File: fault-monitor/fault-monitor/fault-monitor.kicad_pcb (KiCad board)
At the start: 2 copper layers, 72 x 73.5 mm, 25 parts, among them J1 Conn_01x03, J2 Conn_01x06, J3 Conn_01x02, J4 Conn_01x02, J5 Conn_01x02, J6 Conn_01x02, J7 Conn_01x06, U1 ESP32-DevKitC

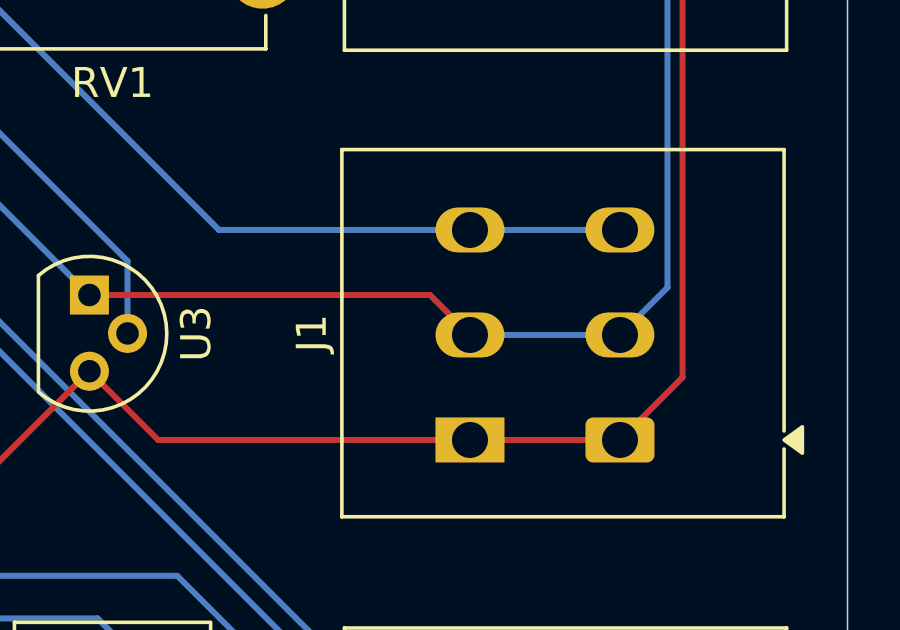
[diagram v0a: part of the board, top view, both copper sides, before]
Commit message: update to use real parts we will order
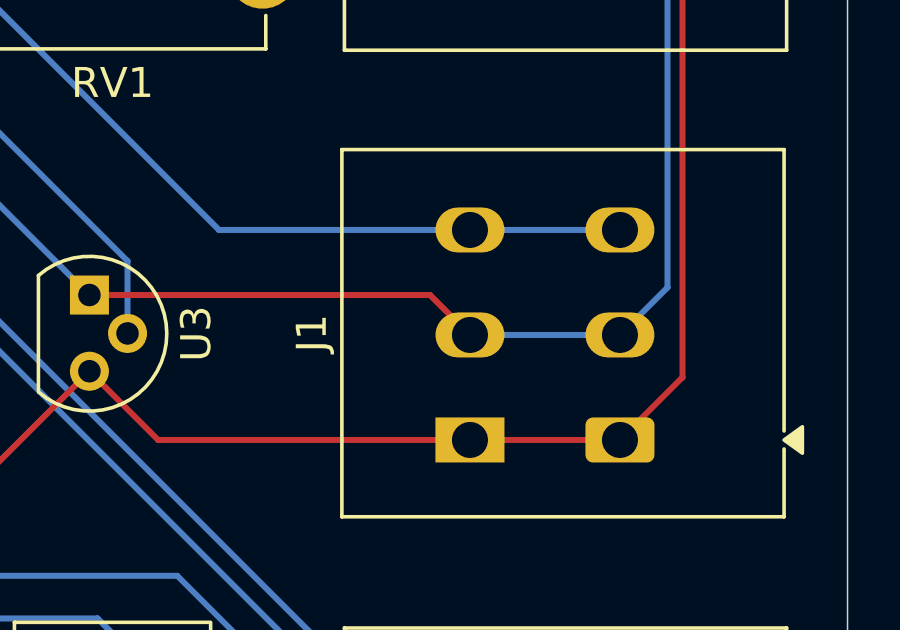
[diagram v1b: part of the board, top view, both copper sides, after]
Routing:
- net GND: track 160.8 -> 158.9 mm
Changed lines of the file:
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@@
-	)
-	(segment
-		(start 110.415 76.05156)
-		(end 109.08344 74.72)
-		(width 0.2)
-		(layer "B.Cu")
-		(net 1)
 	)
 	(segment

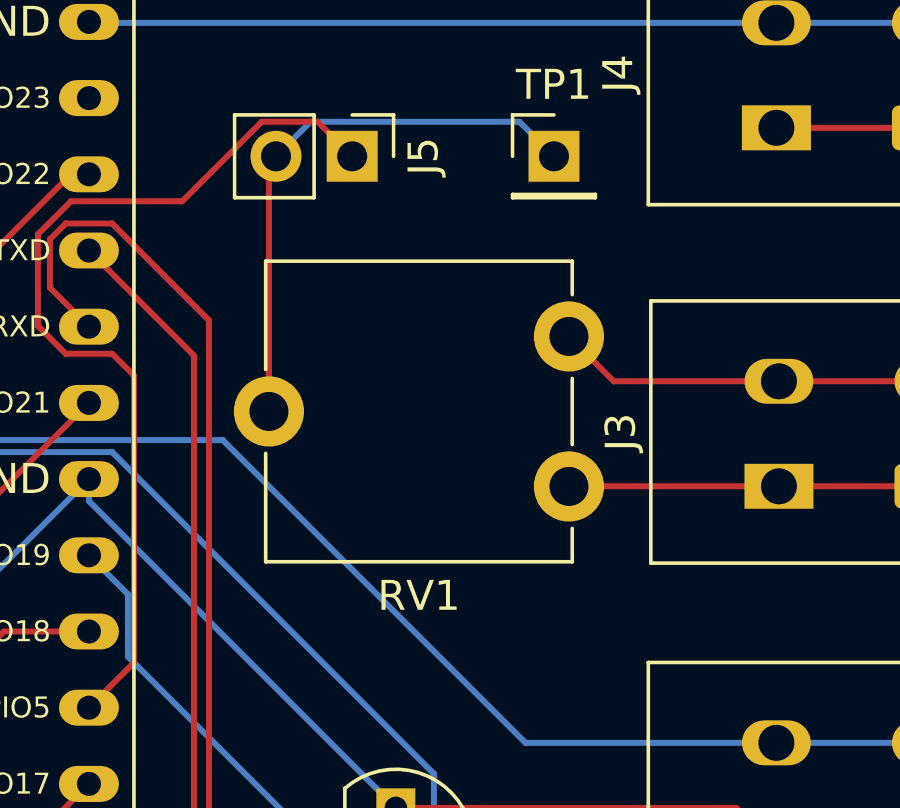
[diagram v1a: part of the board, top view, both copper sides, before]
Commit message: swap pot foot
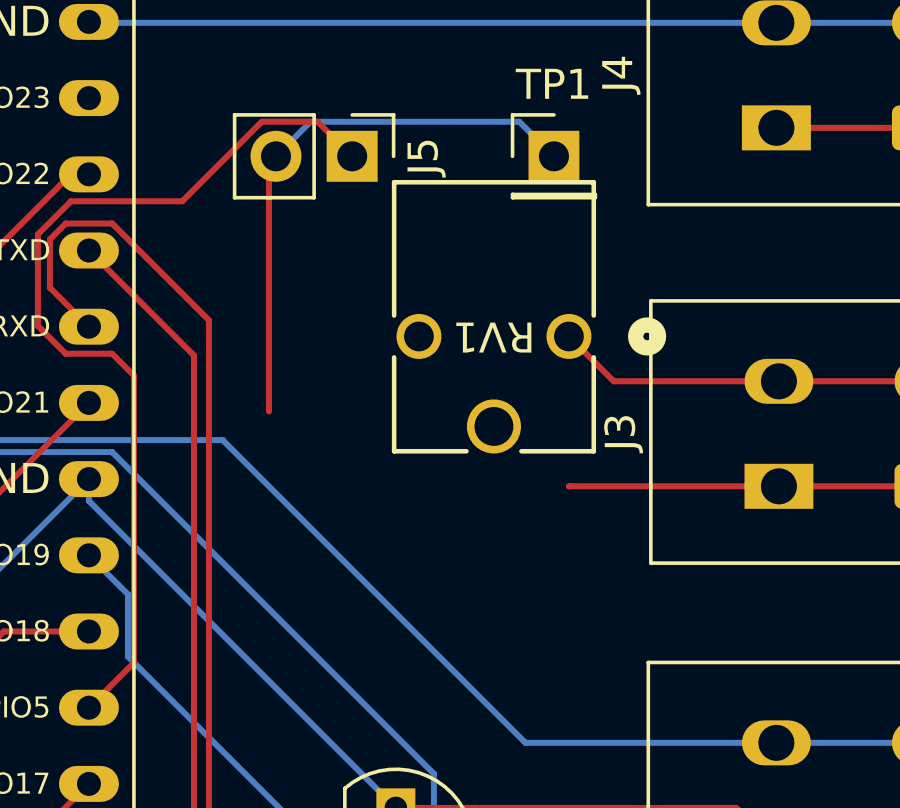
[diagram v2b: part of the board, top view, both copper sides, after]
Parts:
- RV1: footprint Potentiometer_THT:Potentiometer_ACP_CA9-V10_Vertical -> DigiKey:POT_N6L30T0N_AMP
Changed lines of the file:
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@@
 		(embedded_fonts no)
 	)
-	(footprint "Potentiometer_THT:Potentiometer_ACP_CA9-V10_Vertical"
+	(footprint "DigiKey:POT_N6L30T0N_AMP"
 		(layer "F.Cu")
 		(at 103.5 59.005 180)
-		(descr "Potentiometer, vertical, ACP CA9-V10, http://www.acptechnologies.com/wp-content/uploads/2017/05/02-ACP-CA9-CE9.pdf")
-		(tags "Potentiometer vertical ACP CA9-V10")
+		(tags "N6L30T0N-103-3030 ")
 		(property "Reference" "RV1"
-			(at 5 -8.65 0)
+			(at 2.5 0 180)
+			(unlocked yes)
 			(layer "F.SilkS")
 			(effects
@@
 		)
 		(property "Value" "10K"
-			(at 5 3.65 0)
+			(at 2.5 0 180)
+			(unlocked yes)
 			(layer "F.Fab")
 			(effects
@@
 		)
 		(property "Datasheet" "~"
-			(at 0 0 0)
+			(at 0 0 180)
 			(layer "F.Fab")
 			(hide yes)
@@
 		)
 		(property "Description" "Potentiometer"
-			(at 0 0 0)
+			(at 0 0 180)
 			(layer "F.Fab")
 			(hide yes)
@@
 		(attr through_hole)
 		(fp_line
-			(start 10.11 2.51)
-			(end -0.11 2.51)
-			(stroke
-				(width 0.12)
-				(type solid)
-			)
-			(layer "F.SilkS")
-		)
-		(fp_line
-			(start 10.11 -1.104)
-			(end 10.11 2.51)
-			(stroke
-				(width 0.12)
-				(type solid)
-			)
-			(layer "F.SilkS")
-		)
-		(fp_line
-			(start 10.11 -7.51)
-			(end 10.11 -3.896)
-			(stroke
-				(width 0.12)
-				(type solid)
-			)
-			(layer "F.SilkS")
-		)
-		(fp_line
-			(start -0.11 2.51)
-			(end -0.11 1.396)
-			(stroke
-				(width 0.12)
-				(type solid)
-			)
-			(layer "F.SilkS")
-		)
-		(fp_line
-			(start -0.11 -1.396)
-			(end -0.11 -3.604)
-			(stroke
-				(width 0.12)
-				(type solid)
-			)
-			(layer "F.SilkS")
-		)
-		(fp_line
-			(start -0.11 -6.396)
-			(end -0.11 -7.51)
-			(stroke
-				(width 0.12)
-				(type solid)
-			)
-			(layer "F.SilkS")
-		)
-		(fp_line
-			(start -0.11 -7.51)
-			(end 10.11 -7.51)
-			(stroke
-				(width 0.12)
-				(type solid)
-			)
-			(layer "F.SilkS")
-		)
-		(fp_rect
-			(start -1.42 -7.65)
-			(end 11.42 2.66)
-			(stroke
-				(width 0.05)
+			(start 5.8274 5.1392)
+			(end 5.8274 0.697295)
+			(stroke
+				(width 0.1524)
+				(type solid)
+			)
+			(layer "F.SilkS")
+		)
+		(fp_line
+			(start 5.8274 -0.697295)
+			(end 5.8274 -3.827)
+			(stroke
+				(width 0.1524)
+				(type solid)
+			)
+			(layer "F.SilkS")
+		)
+		(fp_line
+			(start 5.8274 -3.827)
+			(end 3.416467 -3.827)
+			(stroke
+				(width 0.1524)
+				(type solid)
+			)
+			(layer "F.SilkS")
+		)
+		(fp_line
+			(start 1.583533 -3.827)
+			(end -0.8274 -3.827)
+			(stroke
+				(width 0.1524)
+				(type solid)
+			)
+			(layer "F.SilkS")
+		)
+		(fp_line
+			(start -0.8274 5.1392)
+			(end 5.8274 5.1392)
+			(stroke
+				(width 0.1524)
+				(type solid)
+			)
+			(layer "F.SilkS")
+		)
+		(fp_line
+			(start -0.8274 0.697295)
+			(end -0.8274 5.1392)
+			(stroke
+				(width 0.1524)
+				(type solid)
+			)
+			(layer "F.SilkS")
+		)
+		(fp_line
+			(start -0.8274 -3.827)
+			(end -0.8274 -0.697295)
+			(stroke
+				(width 0.1524)
+				(type solid)
+			)
+			(layer "F.SilkS")
+		)
+		(fp_circle
+			(center -2.6054 0)
+			(end -2.2244 0)
+			(stroke
+				(width 0.508)
 				(type solid)
 			)
 			(fill no)
-			(layer "F.CrtYd")
-		)
-		(fp_rect
-			(start 0 -7.4)
-			(end 10 2.4)
-			(stroke
-				(width 0.1)
+			(layer "F.SilkS")
+		)
+		(fp_circle
+			(center -2.6054 0)
+			(end -2.2244 0)
+			(stroke
+				(width 0.508)
 				(type solid)
 			)
 			(fill no)
+			(layer "B.SilkS")
+		)
+		(fp_line
+			(start 6.1557 5.2662)
+			(end 6.1557 -4.155699)
+			(stroke
+				(width 0.1524)
+				(type solid)
+			)
+			(layer "F.CrtYd")
+		)
+		(fp_line
+			(start 6.1557 -4.155699)
+			(end -1.1557 -4.155699)
+			(stroke
+				(width 0.1524)
+				(type solid)
+			)
+			(layer "F.CrtYd")
+		)
+		(fp_line
+			(start -1.1557 5.2662)
+			(end 6.1557 5.2662)
+			(stroke
+				(width 0.1524)
+				(type solid)
+			)
+			(layer "F.CrtYd")
+		)
+		(fp_line
+			(start -1.1557 -4.155699)
+			(end -1.1557 5.2662)
+			(stroke
+				(width 0.1524)
+				(type solid)
+			)
+			(layer "F.CrtYd")
+		)
+		(fp_line
+			(start 5.7004 5.0122)
+			(end 5.7004 -3.7)
+			(stroke
+				(width 0.0254)
+				(type solid)
+			)
+			(layer "F.Fab")
+		)
+		(fp_line
+			(start 5.7004 -3.7)
+			(end -0.7004 -3.7)
+			(stroke
+				(width 0.0254)
+				(type solid)
+			)
+			(layer "F.Fab")
+		)
+		(fp_line
+			(start -0.7004 5.0122)
+			(end 5.7004 5.0122)
+			(stroke
+				(width 0.0254)
+				(type solid)
+			)
+			(layer "F.Fab")
+		)
+		(fp_line
+			(start -0.7004 -3.7)
+			(end -0.7004 5.0122)
+			(stroke
+				(width 0.0254)
+				(type solid)
+			)
 			(layer "F.Fab")
 		)
 		(fp_circle
-			(center 5 -2.5)
-			(end 6.05 -2.5)
-			(stroke
-				(width 0.1)
+			(center 0 -1.905)
+			(end 0.381 -1.905)
+			(stroke
+				(width 0.508)
 				(type solid)
 			)
@@
 		)
 		(fp_text user "${REFERENCE}"
-			(at 1 -2.5 90)
+			(at 2.5 0 180)
+			(unlocked yes)
 			(layer "F.Fab")
 			(effects
@@
 		(pad "1" thru_hole circle
 			(at 0 0 180)
-			(size 2.34 2.34)
-			(drill 1.3)
+			(size 1.4986 1.4986)
+			(drill 0.9906)
 			(layers "*.Cu" "*.Mask")
 			(remove_unused_layers no)
@@
 		)
 		(pad "2" thru_hole circle
-			(at 10 -2.5 180)
-			(size 2.34 2.34)
-			(drill 1.3)
+			(at 2.5 -2.999999 180)
+			(size 1.8034 1.8034)
+			(drill 1.2954)
 			(layers "*.Cu" "*.Mask")
 			(remove_unused_layers no)
@@
 		)
 		(pad "3" thru_hole circle
-			(at 0 -5 180)
-			(size 2.34 2.34)
-			(drill 1.3)
+			(at 5 0 180)
+			(size 1.4986 1.4986)
+			(drill 0.9906)
 			(layers "*.Cu" "*.Mask")
 			(remove_unused_layers no)
@@
 		)
 		(embedded_fonts no)
-		(model "${KICAD9_3DMODEL_DIR}/Potentiometer_THT.3dshapes/Potentiometer_ACP_CA9-V10_Vertical.step"
-			(offset
-				(xyz 0 0 0)
-			)
-			(scale
-				(xyz 1 1 1)
-			)
-			(rotate
-				(xyz 0 0 0)
-			)
-		)
 	)
 	(footprint "Resistor_THT:R_Axial_DIN0207_L6.3mm_D2.5mm_P10.16mm_Horizontal"

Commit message: full redo of pcb cuz we fucked up the usb port
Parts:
- removed the REF** at (120.5, 43.0)
- removed the REF** at (53.5, 111.5)
- removed the REF** at (53.5, 43.0)
- removed the REF** at (120.5, 111.5)
- added REF**: MountingHole_2.2mm_M2, MountingHole:MountingHole_2.2mm_M2, F.Cu at (61.5, 27.5)
- added REF**: MountingHole_2.2mm_M2, MountingHole:MountingHole_2.2mm_M2, F.Cu at (92.0, 80.0)
- J1: footprint TerminalBlock_WAGO_3D:TerminalBlock_WAGO_2601-1103_1x03_P3.50mm_Horizontal-3D -> TerminalBlock:TerminalBlock_MaiXu_MX126-5.0-03P_1x03_P5.00mm
- J2, J7: footprint TerminalBlock_WAGO_3D:TerminalBlock_WAGO_2601-1106_1x06_P3.50mm_Horizontal-3D -> TerminalBlock:TerminalBlock_MaiXu_MX126-5.0-06P_1x06_P5.00mm
- J3, J4, J6: footprint TerminalBlock_WAGO_3D:TerminalBlock_WAGO_2601-1102_1x02_P3.50mm_Horizontal-3D -> TerminalBlock:TerminalBlock_MaiXu_MX126-5.0-02P_1x02_P5.00mm
- moved J2 100.0 mm to (53.0, 28.0), turned to -90 degrees
- moved R2 91.2 mm to (100.5, 29.2), turned to -90 degrees
- moved R1 87.7 mm to (97.3, 29.2), turned to -90 degrees
- moved J4 72.0 mm to (53.0, 88.0), turned to -90 degrees
- moved J1 65.5 mm to (53.0, 59.8), turned to -90 degrees
- moved D2 65.1 mm to (100.3, 44.2), turned to 180 degrees
- moved J3 63.7 mm to (53.0, 76.5), turned to -90 degrees
- moved R3 58.5 mm to (100.5, 82.6), turned to 90 degrees
- moved D1 55.3 mm to (100.3, 52.1), turned to 180 degrees
- moved R4 52.9 mm to (97.3, 82.6), turned to 90 degrees
- moved D4 48.8 mm to (100.3, 59.9), turned to 180 degrees
- moved D3 46.9 mm to (100.3, 67.7), turned to 180 degrees
- moved RV1 46.8 mm to (63.9, 84.0), turned to 90 degrees
- moved R5 44.0 mm to (63.0, 59.1), turned to 90 degrees
- moved R6 43.9 mm to (59.5, 59.1), turned to 90 degrees
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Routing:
- net /STOPALL: track 107.0 -> 56.8 mm
- net GND: track 158.9 -> 115.6 mm
- net /IO22: track 63.9 -> 25.8 mm
- net /IO0: track 28.3 -> 63.1 mm
- net Net-(J6-Pin_2): track 61.1 -> 27.2 mm
- net Net-(J6-Pin_1): track 53.3 -> 26.4 mm
- net /IO4: track 32.3 -> 58.5 mm
- net /SOFTSTART: track 41.2 -> 17.4 mm
- net /FAN: track 43.7 -> 20.2 mm
- net /IO21: track 54.4 -> 34.5 mm
- net /RELAY: track 34.6 -> 15.3 mm
- net /ALARMLEFT: track 56.7 -> 43.6 mm
- net Net-(U1-IO25): track 42.0 -> 29.1 mm
- net Net-(U1-IO26): track 37.8 -> 25.2 mm
- net /IO17: track 38.8 -> 51.3 mm
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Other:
- board size 72 x 73.5 mm -> 54.5 x 72 mm
- board text removed: "0"
- board text removed: "17"
- board text removed: "18"
- board text removed: "21"
- board text removed: "22"
- board text removed: "24V"
- board text removed: "24V REF"
- board text removed: "4"
- board text removed: "5V"
- board text removed: "5V PWR"
- board text removed: "ALL"
- board text removed: "ALR"
- board text removed: "CURR. SENS."
- board text removed: "FAN"
- board text removed: "GND"
- board text removed: "GPIO"
- board text removed: "IN"
- board text removed: "REL"
- board text removed: "RX"
- board text removed: "SNS"
- board text removed: "SST"
- board text removed: "STP"
- board text removed: "TX"

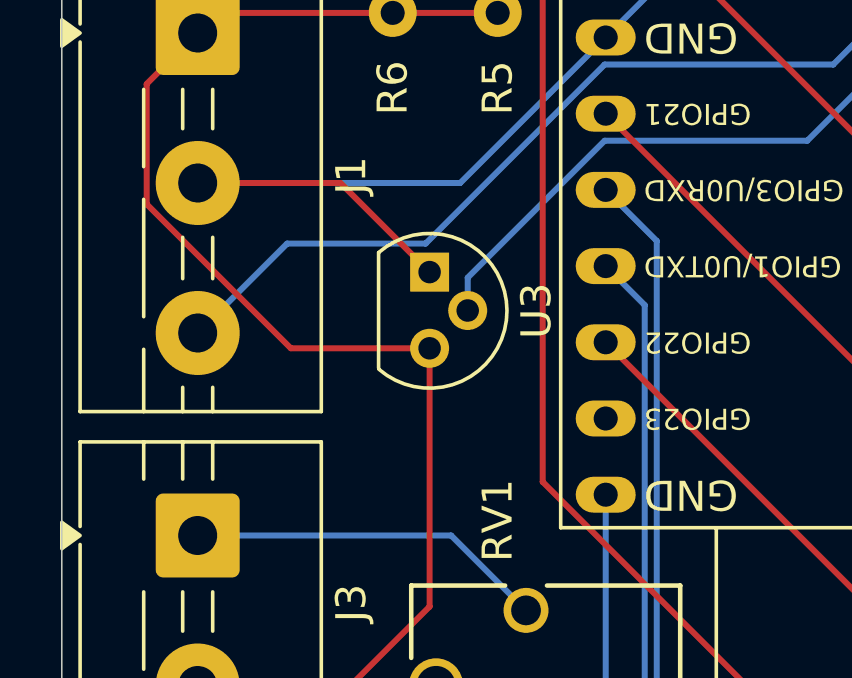
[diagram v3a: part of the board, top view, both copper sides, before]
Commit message: missed a trace
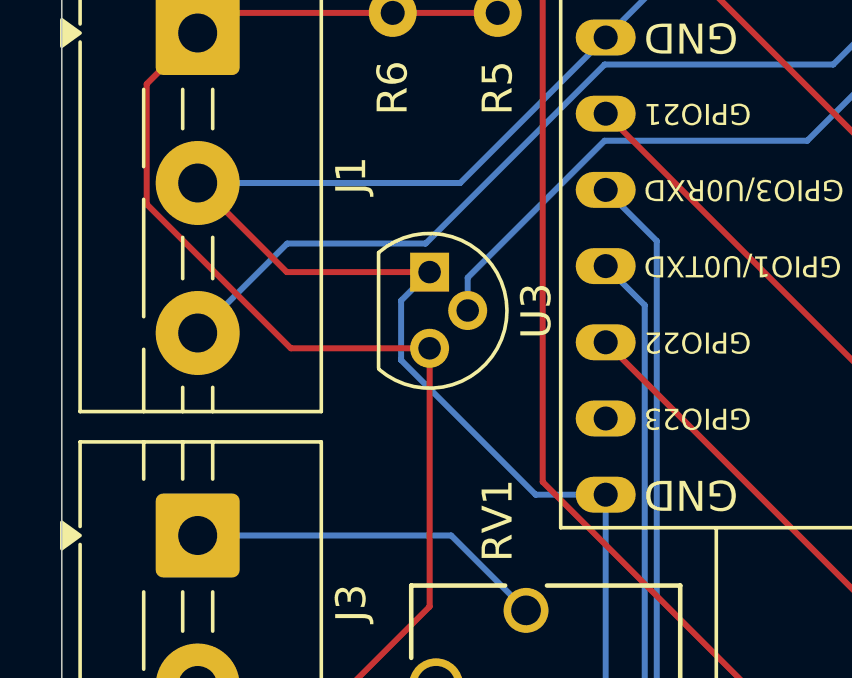
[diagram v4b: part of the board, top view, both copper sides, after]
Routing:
- net GND: track 115.6 -> 127.6 mm
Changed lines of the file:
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@@
 	)
 	(segment
-		(start 53 64.75)
-		(end 57.76 64.75)
+		(start 55.97 67.72)
+		(end 60.73 67.72)
 		(width 0.2)
 		(layer "F.Cu")
@@
 	)
 	(segment
-		(start 57.76 64.75)
-		(end 60.73 67.72)
+		(start 53 64.75)
+		(end 55.97 67.72)
 		(width 0.2)
 		(layer "F.Cu")
+		(net 1)
+	)
+	(segment
+		(start 64.265082 75.14)
+		(end 66.6 75.14)
+		(width 0.2)
+		(layer "B.Cu")
 		(net 1)
 	)
@@
 	)
 	(segment
+		(start 59.779 70.653918)
+		(end 64.265082 75.14)
+		(width 0.2)
+		(layer "B.Cu")
+		(net 1)
+	)
+	(segment
 		(start 98.22344 42.12)
 		(end 92 42.12)
+		(width 0.2)
+		(layer "B.Cu")
+		(net 1)
+	)
+	(segment
+		(start 59.779 68.671)
+		(end 59.779 70.653918)
 		(width 0.2)
 		(layer "B.Cu")
@@
 		(width 0.2)
 		(layer "B.Cu")
+		(net 1)
+	)
+	(segment
+		(start 60.73 67.72)
+		(end 59.779 68.671)
+		(width 0.2)
+		(layer "B.Cu")

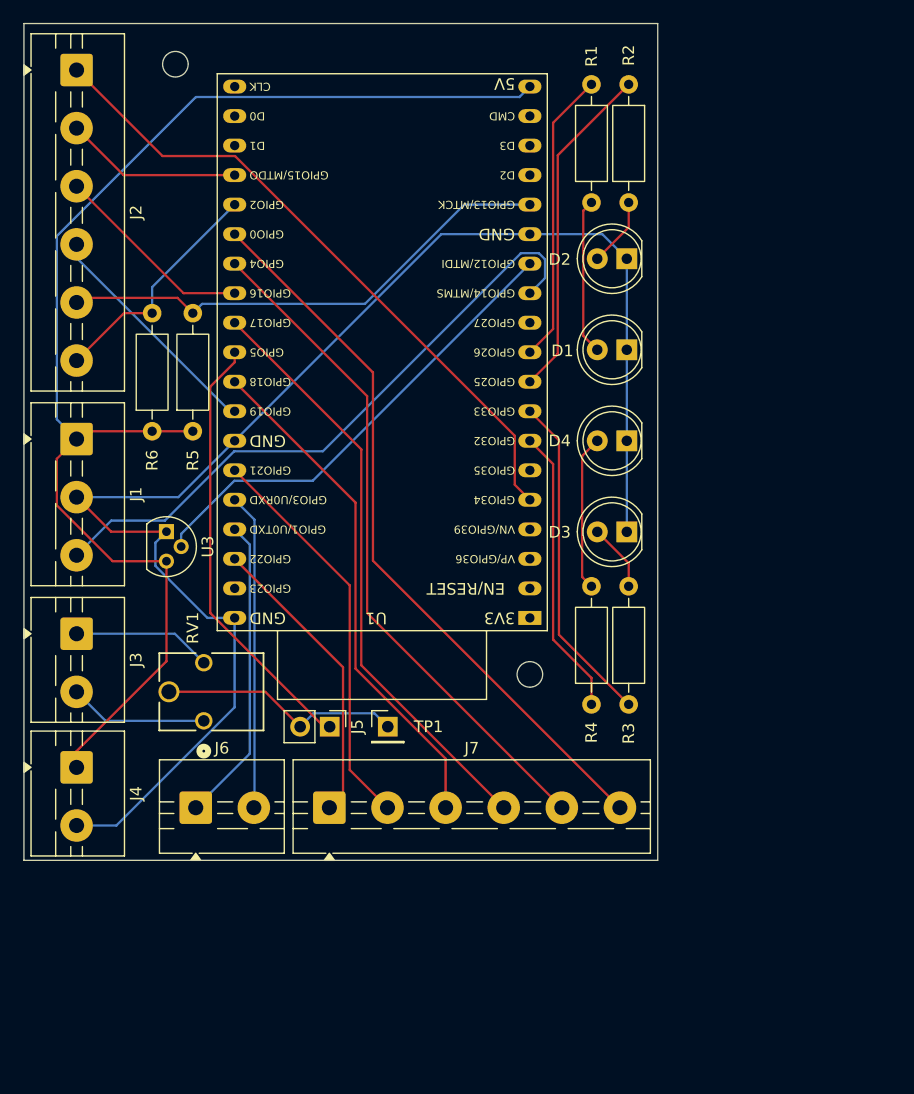
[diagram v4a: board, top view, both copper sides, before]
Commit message: increase hole size for esp32, redo routing
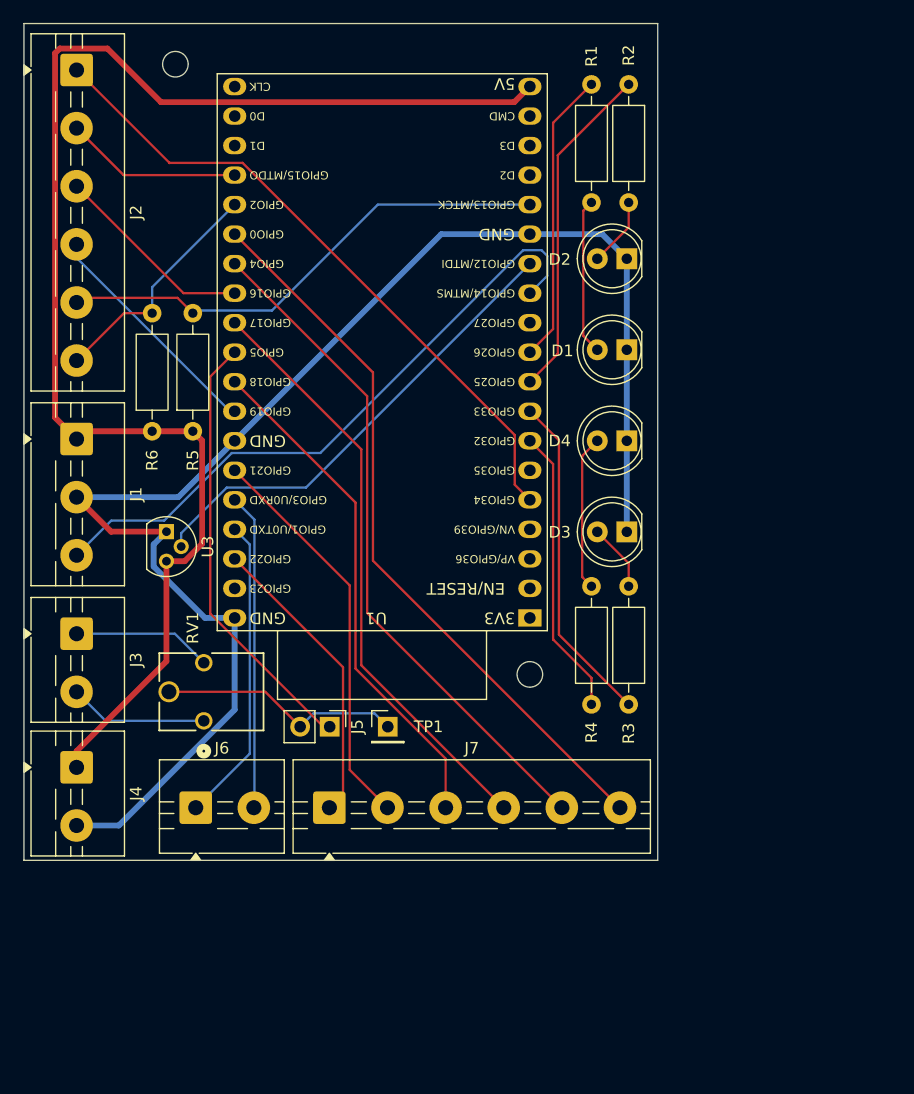
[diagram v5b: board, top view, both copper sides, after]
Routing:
- net +5V: track 113.2 -> 122.4 mm
- net Net-(J1-Pin_3): track 54.7 -> 55.4 mm
